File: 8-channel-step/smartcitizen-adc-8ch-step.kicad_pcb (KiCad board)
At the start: 2 copper layers, 56.6 x 64.7 mm, 51 parts, among them J1 GROVE1, J2 GROVE2, J4 USB_BULGIN, J5 Conn_02x05_Odd_Even, J6 USB_B_Micro, J7 USB_A, M1 PINHD-1x06-HEADER, M2 PINHD-1x06-HEADER, M3 PINHD-1x06-HEADER, M4 PINHD-1x06-HEADER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

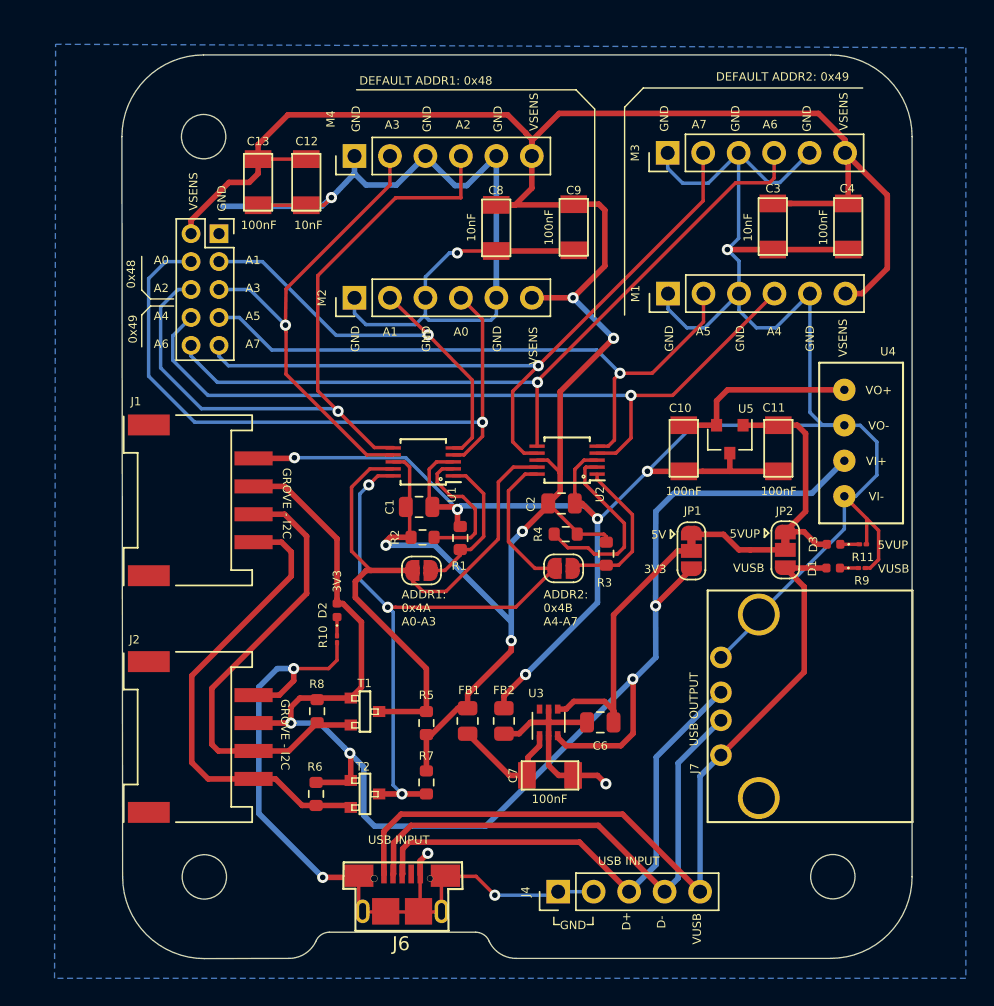
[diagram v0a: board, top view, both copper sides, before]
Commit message: Add reduced 8-channel step-up version
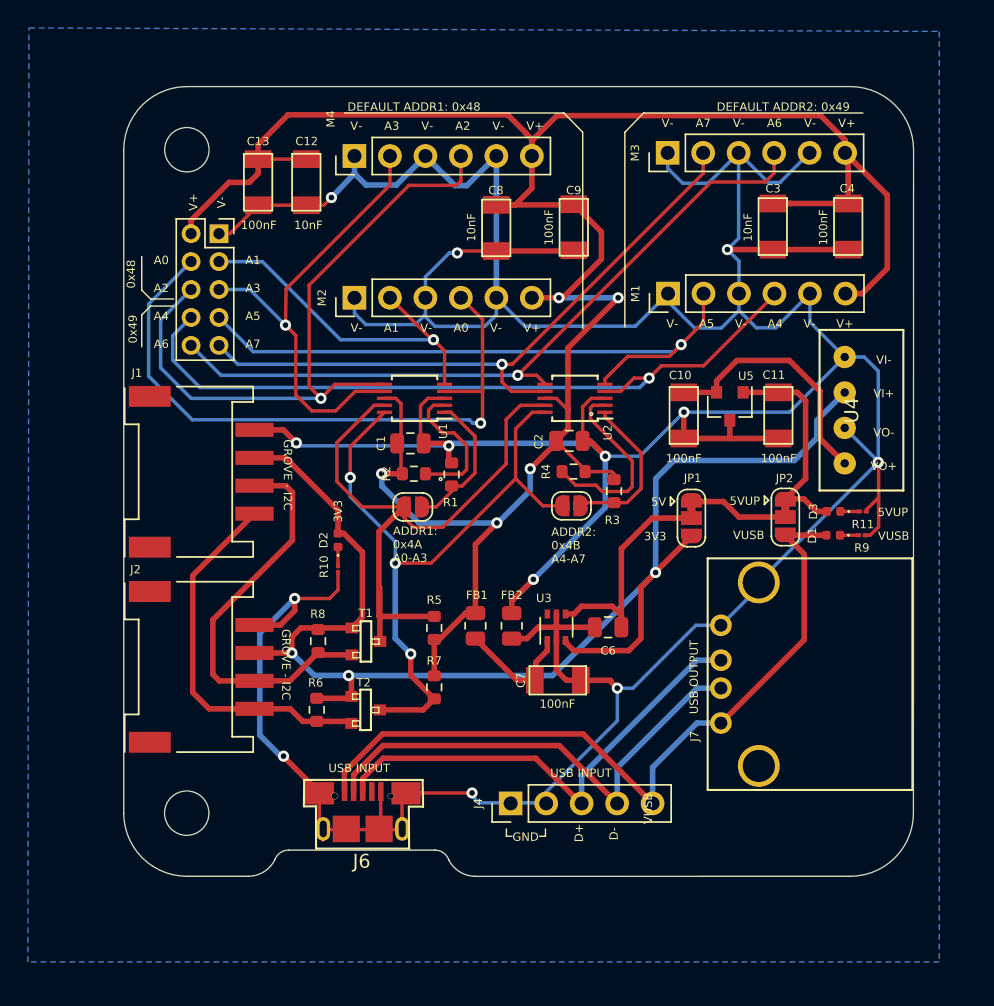
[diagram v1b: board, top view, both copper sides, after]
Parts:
- moved J4 7.18 mm to (153.7, 111.8)
- moved C6 6.83 mm to (160.7, 99.2)
- moved C7 6.83 mm to (157.1, 103.0)
- moved FB1 6.83 mm to (151.2, 99.1)
- moved FB2 6.83 mm to (153.8, 99.1)
- moved R5 6.83 mm to (148.2, 99.2)
- moved R7 6.83 mm to (148.2, 103.5)
- moved U3 6.83 mm to (157.0, 99.2)
- moved J6 6.54 mm to (143.1, 112.3)
- moved T2 6.02 mm to (143.3, 105.1)
- moved R6 6.02 mm to (139.8, 105.1)
- moved R8 5.02 mm to (139.9, 100.2)
- moved D2 5.02 mm to (141.3, 93.0)
- moved J2 5.02 mm to (130.5, 102.0)
- moved R10 5.02 mm to (141.3, 95.0)
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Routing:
- net GND: track 324.7 -> 338.7 mm
- net VGROVE: track 108.5 -> 98.1 mm, vias 4 -> 3
- net VCC: track 177.2 -> 169.6 mm
- net SCL3V3: track 33.7 -> 26.7 mm
- net A1: track 31.3 -> 25.6 mm
- net A7: track 52.3 -> 47.0 mm
- net Net-(C10-Pad1): track 13.6 -> 18.0 mm
- net A2: track 52.3 -> 48.3 mm
- net SDA3V3: track 33.2 -> 29.3 mm
- net VUSB: track 58.5 -> 54.7 mm
- net VCC_PRE: track 21.3 -> 17.7 mm
- net A6: track 55.8 -> 52.3 mm
- net D-: track 38.1 -> 35.0 mm
- net D+: track 36.8 -> 33.9 mm
- net SCL: track 52.5 -> 49.7 mm
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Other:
- board size 56.6 x 64.7 mm -> 56.6 x 56.5 mm
- board text added: "11/06/2021"
- board text added: "V+"
- board text added: "V-"
- board text removed: "17/05/2021"
- board text removed: "VSENS"

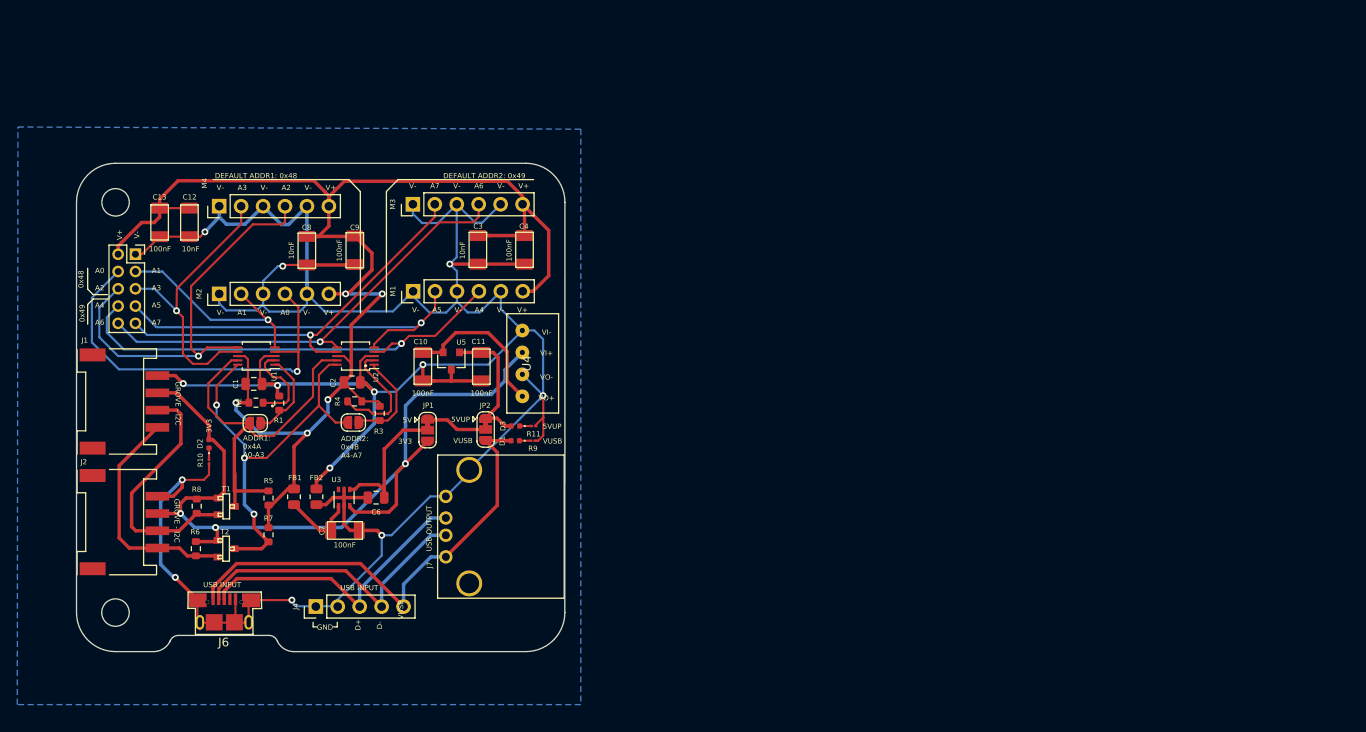
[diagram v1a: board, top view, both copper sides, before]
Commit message: Stable version fixing address issue
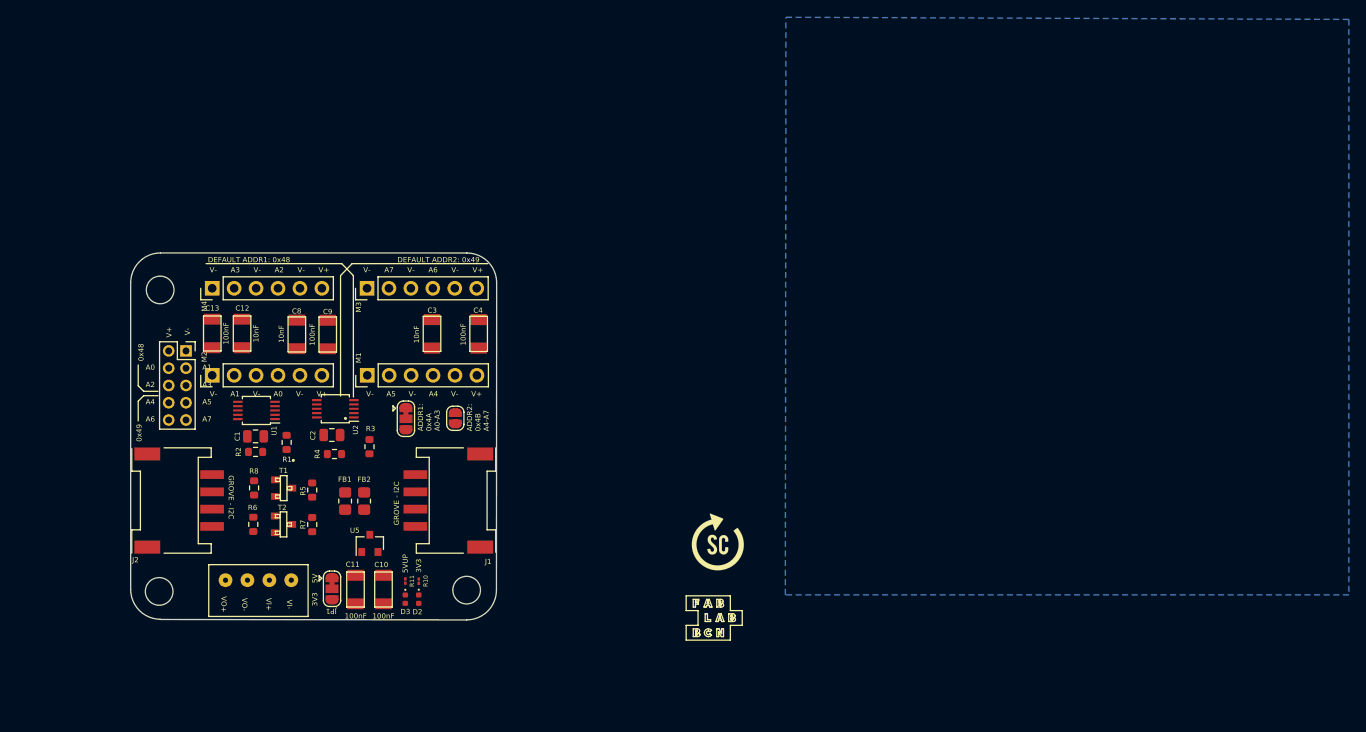
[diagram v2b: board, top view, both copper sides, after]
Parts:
- removed C6: 1uF, Capacitor_SMD:C_0805_2012Metric
- removed C7: 100nF, fab-C1206FAB
- removed D1: RED_LED, LED_SMD:LED_0402_1005Metric
- removed J4: USB_BULGIN, Connector_PinHeader_2.54mm:PinHeader_1x05_P2.54mm_Vertical
- removed J6: USB_B_Micro, Connector_USB:USB_Micro-B_XKB-U254-051T-4BH83-F1S_Horizontal
- removed J7: USB_A, Connector_USB:USB_A_Amphenol_87520-1110BLF
- removed JP1: J3_Bridged12, Jumper:SolderJumper-3_P1.3mm_Bridged12_RoundedPad1.0x1.5mm
- removed R9: 1kΩ, Resistor_SMD:R_01005_0402Metric
- removed U3: SiP32431DR3, Package_TO_SOT_SMD:SOT-363_SC-70-6
- added H1: MountingHole, MountingHole:MountingHole_3.2mm_M3, F.Cu at (135.6, 110.0)
- added H2: MountingHole, MountingHole:MountingHole_3.2mm_M3, F.Cu at (135.7, 75.1)
- added H3: MountingHole, MountingHole:MountingHole_3.2mm_M3, F.Cu at (171.2, 109.9)
- added OSH1: Logo_Open_Hardware_Small, Symbol:OSHW-Symbol_6.7x6mm_SilkScreen, B.Cu at (176.9, 101.8)
- FB1, FB2: footprint Resistor_SMD:R_0805_2012Metric -> Resistor_SMD:R_0805_2012Metric_Pad1.20x1.40mm_HandSolder
- JP2: value Jumper_2_Open -> J3_Bridged12; footprint Jumper:SolderJumper-2_P1.3mm_Open_RoundedPad1.0x1.5mm -> Jumper:SolderJumper-3_P1.3mm_Bridged12_RoundedPad1.0x1.5mm
- LO1, LO2: moved to F.Cu
- moved LO1 71.1 mm to (200.4, 104.3), turned to 0 degrees
- moved LO2 65.1 mm to (199.5, 117.5), turned to 0 degrees
- moved J1 41.1 mm to (170.0, 99.5), turned to 270 degrees
- moved U4 39.5 mm to (147.0, 108.8), turned to 0 degrees
- moved D2 30.2 mm to (165.6, 110.9), turned to 270 degrees
- moved C11 29.6 mm to (158.3, 109.8)
- moved R10 28.0 mm to (165.6, 108.9), turned to 270 degrees
- moved C10 26.2 mm to (161.5, 109.8)
- moved D3 23.8 mm to (164.1, 111.0), turned to 270 degrees
- moved R11 23.3 mm to (164.1, 108.8), turned to 270 degrees
- moved U5 23.1 mm to (159.9, 104.5), turned to 90 degrees
- moved JP4 21.4 mm to (155.6, 109.7)
- moved JP2 17.4 mm to (164.1, 90.1), turned to 270 degrees
- moved C12 14.2 mm to (145.2, 80.2)
- moved C13 14.2 mm to (141.7, 80.2)
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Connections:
- FB1 pad 2: Net-(C7-Pad1) -> Net-(FB1-Pad2)
- JP2 pad 1: ADDR1 -> Net-(JP2-Pad1)
- JP2 pad 2: SDA -> ADDR1
- JP4 pad 1: 5VSEL -> 5VGROVE
- JP4 pad 2: VCC_PRE -> Net-(FB1-Pad2)
- R1 pad 1: ADDR1 -> Net-(JP2-Pad1)
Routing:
- net GND: track 338.7 -> 0.00 mm, vias 13 -> 0
- net VCC: track 169.6 -> 0.00 mm, vias 5 -> 0
- net VGROVE: track 98.1 -> 0.00 mm, vias 3 -> 0
- net VUSB: track 54.7 -> 0.00 mm
- net A4: track 53.9 -> 0.00 mm, vias 1 -> 0
- net A6: track 52.3 -> 0.00 mm, vias 1 -> 0
- net SCL: track 49.7 -> 0.00 mm, vias 3 -> 0
- net A2: track 48.3 -> 0.00 mm, vias 1 -> 0
- net A0: track 47.0 -> 0.00 mm, vias 1 -> 0
- net A7: track 47.0 -> 0.00 mm, vias 1 -> 0
- net SDA: track 45.8 -> 0.00 mm
- net A5: track 45.5 -> 0.00 mm, vias 1 -> 0
- net D-: track 35.0 -> 0.00 mm
- net D+: track 33.9 -> 0.00 mm
- net A3: track 33.7 -> 0.00 mm, vias 1 -> 0
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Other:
- board size 56.6 x 56.5 mm -> 42.4 x 42.5 mm
- net class Default: clearance 0.2 -> 0.19812
- rule trace_clearance: 0.2 -> 0.19812
- board text added: "05/07/2021"
- board text added: "I2C-V: 3.3V Power configurations: - 3V3 Grove (JP1-3V3) - 5V DC/DC Step up (JP1-5V)"
- board text removed: "11/06/2021"
- board text removed: "D+"
- board text removed: "D-"
- board text removed: "GND"
- board text removed: "I2C-V: 3.3V to EXT-V EXT-V: I2C-V to 5.5V Power configurations: - 3V3 Grove (JP1-3V3) - 5V DC/DC Step up (JP1-5V, JP2-5VUP) - 5V USB input (JP1-5V, JP2-VUSB) USB Output only when USB Input is provided"
- board text removed: "JP2"
- board text removed: "USB INPUT"
- board text removed: "USB OUTPUT"
- board text removed: "VUSB"
